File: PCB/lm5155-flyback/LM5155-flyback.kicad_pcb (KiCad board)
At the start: 2 copper layers, 2 parts, among them T1 EP7-5801_750315825, U1 LM5155

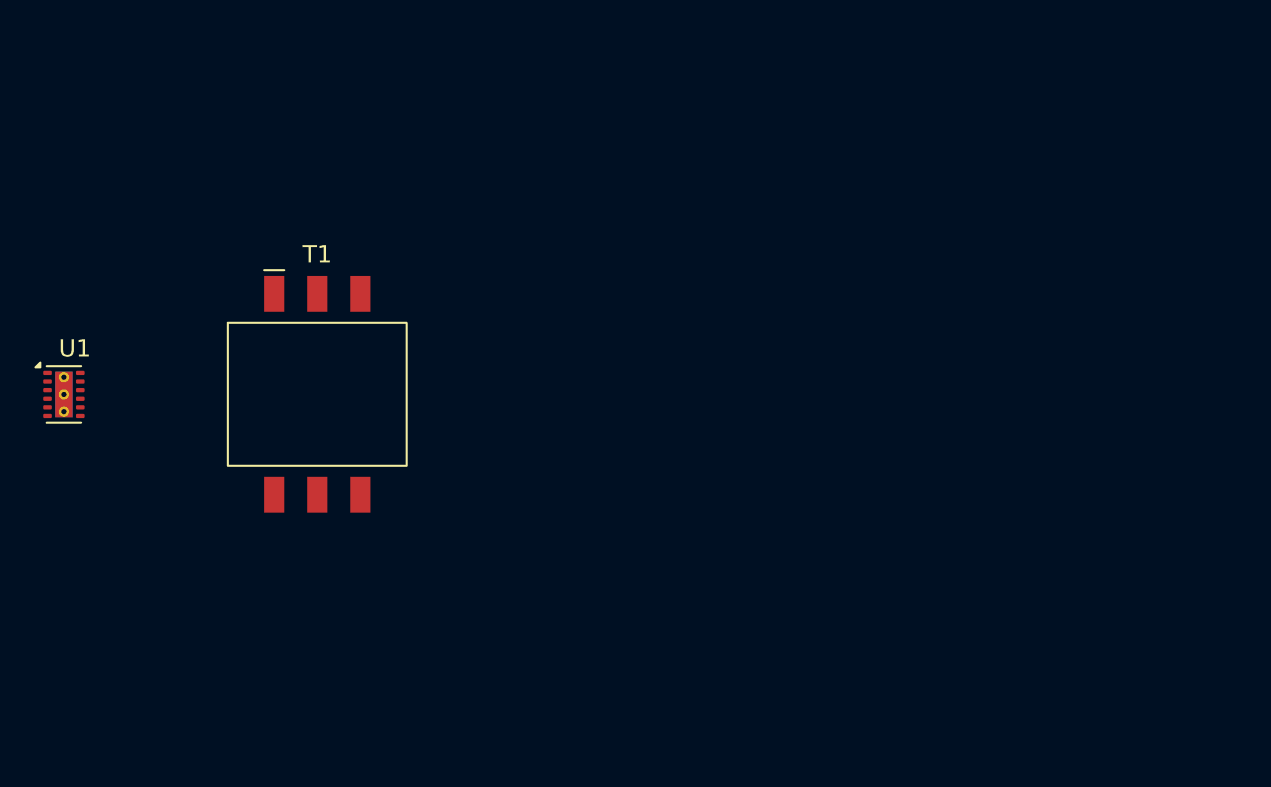
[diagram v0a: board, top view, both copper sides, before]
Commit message: Started flyback layout and tweak simulations
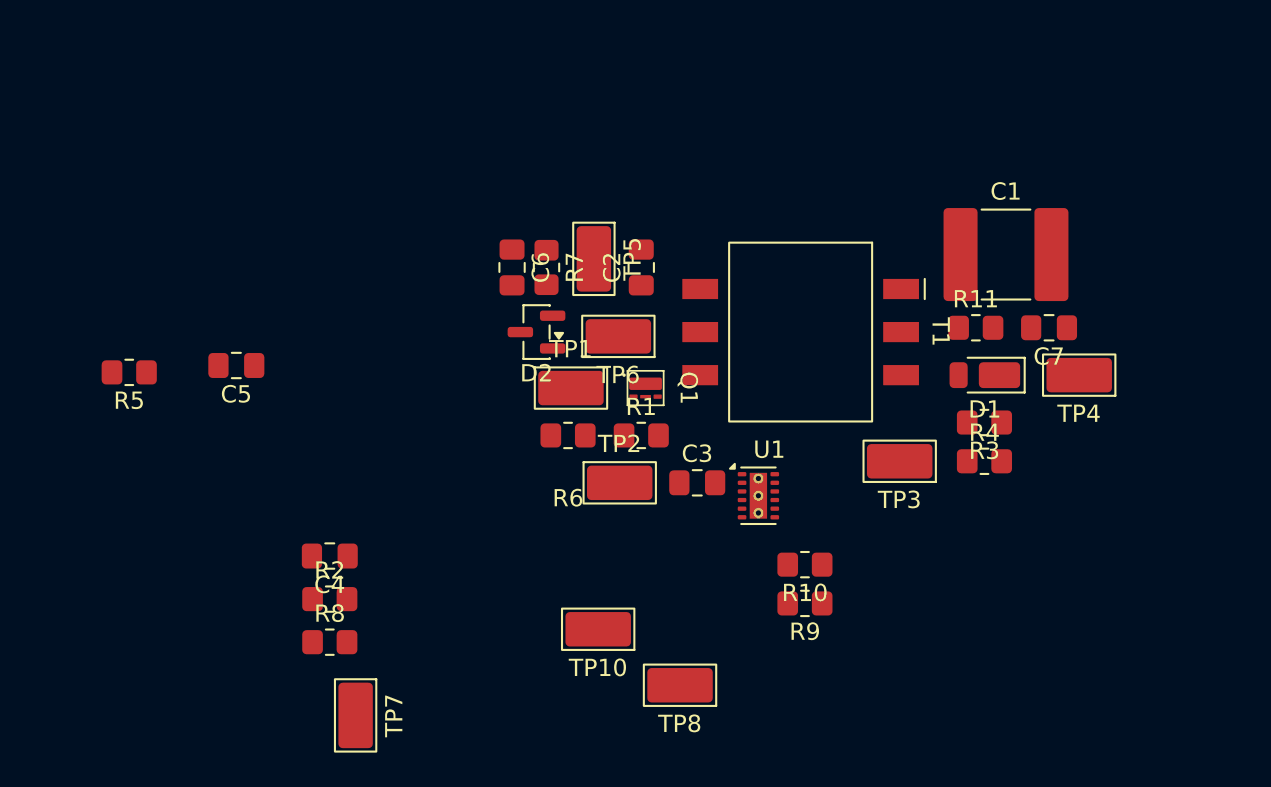
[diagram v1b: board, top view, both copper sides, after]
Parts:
- added C1: 1u, Capacitor_SMD:C_2220_5750Metric_Pad1.97x5.40mm_HandSolder, F.Cu at (192.7, 93.5)
- added C2: 4.7u, Capacitor_SMD:C_0805_2012Metric_Pad1.18x1.45mm_HandSolder, F.Cu at (171.5, 94.2)
- added C3: 1uF, Capacitor_SMD:C_0805_2012Metric_Pad1.18x1.45mm_HandSolder, F.Cu at (174.8, 106.8)
- added C4: 30n, Capacitor_SMD:C_0805_2012Metric_Pad1.18x1.45mm_HandSolder, F.Cu at (153.4, 111.0)
- added C5: 1.6n, Capacitor_SMD:C_0805_2012Metric_Pad1.18x1.45mm_HandSolder, F.Cu at (148.0, 99.9)
- added C6: 5n, Capacitor_SMD:C_0805_2012Metric_Pad1.18x1.45mm_HandSolder, F.Cu at (164.0, 94.2)
- added C7: C, Capacitor_SMD:C_0805_2012Metric_Pad1.18x1.45mm_HandSolder, F.Cu at (195.2, 97.8)
- added D1: SBR1U400P1, Diode_SMD:D_PowerDI-123, F.Cu at (191.4, 100.5)
- added D2: BAS70, Package_TO_SOT_SMD:SOT-23, F.Cu at (165.4, 98.0)
- added Q1: DMT6030LFCL-7, LM5155-flyback:U-DFN1616-6, F.Cu at (171.8, 101.2)
- added R1: 2m, Resistor_SMD:R_0805_2012Metric_Pad1.20x1.40mm_HandSolder, F.Cu at (171.5, 104.0)
- added R10: 43k, Resistor_SMD:R_0805_2012Metric_Pad1.20x1.40mm_HandSolder, F.Cu at (181.0, 111.5)
- added R11: R, Resistor_SMD:R_0805_2012Metric_Pad1.20x1.40mm_HandSolder, F.Cu at (190.9, 97.8)
- added R2: 87.5k, Resistor_SMD:R_0805_2012Metric_Pad1.20x1.40mm_HandSolder, F.Cu at (153.4, 113.5)
- added R3: 1Meg, Resistor_SMD:R_0805_2012Metric_Pad1.20x1.40mm_HandSolder, F.Cu at (191.4, 103.2)
- added R4: 5.6k, Resistor_SMD:R_0805_2012Metric_Pad1.20x1.40mm_HandSolder, F.Cu at (191.4, 105.5)
- added R5: 10k, Resistor_SMD:R_0805_2012Metric_Pad1.20x1.40mm_HandSolder, F.Cu at (141.8, 100.3)
- added R6: 1, Resistor_SMD:R_0805_2012Metric_Pad1.20x1.40mm_HandSolder, F.Cu at (167.2, 104.0)
- added R7: 3.8k, Resistor_SMD:R_0805_2012Metric_Pad1.20x1.40mm_HandSolder, F.Cu at (166.0, 94.2)
- added R8: 100k, Resistor_SMD:R_0805_2012Metric_Pad1.20x1.40mm_HandSolder, F.Cu at (153.4, 116.0)
- added R9: 82k, Resistor_SMD:R_0805_2012Metric_Pad1.20x1.40mm_HandSolder, F.Cu at (181.0, 113.8)
- added TP1: TestPoint, TestPoint:TestPoint_Keystone_5019_Miniature, F.Cu at (167.4, 101.2)
- added TP10: TestPoint, TestPoint:TestPoint_Keystone_5019_Miniature, F.Cu at (169.0, 115.2)
- added TP2: TestPoint, TestPoint:TestPoint_Keystone_5019_Miniature, F.Cu at (170.2, 106.8)
- added TP3: TestPoint, TestPoint:TestPoint_Keystone_5019_Miniature, F.Cu at (186.5, 105.5)
- added TP4: TestPoint, TestPoint:TestPoint_Keystone_5019_Miniature, F.Cu at (196.9, 100.5)
- added TP5: TestPoint, TestPoint:TestPoint_Keystone_5019_Miniature, F.Cu at (168.8, 93.8)
- added TP6: TestPoint, TestPoint:TestPoint_Keystone_5019_Miniature, F.Cu at (170.2, 98.2)
- added TP7: TestPoint, TestPoint:TestPoint_Keystone_5019_Miniature, F.Cu at (154.9, 120.2)
- added TP8: TestPoint, TestPoint:TestPoint_Keystone_5019_Miniature, F.Cu at (173.8, 118.5)
- moved U1 40.7 mm to (178.3, 107.5)
- moved T1 28.3 mm to (180.8, 98.0), turned to -90 degrees
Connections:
- net Net-(U1-BIAS) renamed /VIN
- T1 pad 4: unconnected-(T1-Pad4) -> /SW
- U1 pad 10: Net-(U1-RT) -> /RT
- U1 pad 11: unconnected-(U1-PGOOD-Pad11) -> /PGOOD
- U1 pad 12: unconnected-(U1-UVLO/EN/SYNC-Pad12) -> /UVLO
- U1 pad 3: unconnected-(U1-GATE-Pad3) -> Net-(U1-GATE)
- U1 pad 5: Net-(U1-CS) -> /CS
- U1 pad 6: unconnected-(U1-COMP-Pad6) -> /COMP
- U1 pad 9: Net-(U1-SS) -> /SS

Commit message: More flyback layout. Almost done!
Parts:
- removed TP10, TP7: TestPoint, TestPoint:TestPoint_Keystone_5019_Miniature
- moved R5 38.1 mm to (178.5, 110.5), turned to 0 degrees
- moved C5 33.0 mm to (178.5, 112.5)
- moved R2 30.6 mm to (183.8, 109.5), turned to 90 degrees
- moved R8 30.4 mm to (182.2, 106.5), turned to 180 degrees
- moved C4 28.1 mm to (181.5, 109.5), turned to -90 degrees
- moved R9 9.65 mm to (178.2, 104.5), turned to 0 degrees
- moved R10 7.11 mm to (182.2, 104.5), turned to 0 degrees
- moved TP8 6.27 mm to (174.2, 112.2)
- moved TP2 3.34 mm to (171.0, 103.5), turned to 180 degrees
- moved TP3 2.46 mm to (187.5, 107.8), turned to -90 degrees
- moved R1 2.30 mm to (171.0, 106.2), turned to 180 degrees
- moved TP1 1.61 mm to (166.0, 102.0)
- moved R6 1.50 mm to (167.2, 105.5), turned to 90 degrees
- moved C3 0.56 mm to (175.0, 107.2), turned to 90 degrees
- moved Q1 0.50 mm to (171.8, 100.8)
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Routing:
- net /FB: track 0.00 -> 15.6 mm
- net /VOUT: track 0.00 -> 15.1 mm
- net /VIN: track 0.00 -> 11.8 mm
- net Net-(U1-GATE): track 0.00 -> 11.0 mm
- net /GATE: track 0.00 -> 8.42 mm
- net /CS: track 0.00 -> 8.32 mm, vias 0 -> 2
- net Net-(D1-A): track 0.00 -> 6.09 mm
- net /COMP: track 0.00 -> 5.79 mm
- net /RT: track 0.00 -> 5.02 mm
- net Net-(D2-K): track 0.00 -> 4.93 mm
- net /SW: track 0.00 -> 4.29 mm
- net /UVLO: track 0.00 -> 3.75 mm
- net Net-(U1-VCC): track 0.00 -> 2.57 mm
- net GND: track 0.00 -> 2.57 mm
- net /SS: track 0.00 -> 2.55 mm
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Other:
- board outline added: 48 x 27.5 mm

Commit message: Layout done. Send to fabricate
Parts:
- added REF**: Symbol_HighVoltage_NoTriangle_2x5mm_Copper, Symbol:Symbol_HighVoltage_NoTriangle_2x5mm_Copper, F.Cu at (194.8, 86.8)
- added REF**: MountingHole_4mm, MountingHole:MountingHole_4mm, F.Cu at (201.2, 85.2)
- added REF**: MountingHole_4mm, MountingHole:MountingHole_4mm, F.Cu at (201.2, 111.2)
- added REF**: MountingHole_4mm, MountingHole:MountingHole_4mm, F.Cu at (162.0, 85.2)
- added REF**: OSHW-Logo_5.7x6mm_SilkScreen, Symbol:OSHW-Logo_5.7x6mm_SilkScreen, F.Cu at (169.0, 86.8)
- added REF**: MountingHole_4mm, MountingHole:MountingHole_4mm, F.Cu at (162.0, 111.2)
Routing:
- net /VIN: track 11.8 -> 34.2 mm, vias 0 -> 1
- net /VOUT: track 15.1 -> 22.8 mm, vias 0 -> 1
- net GND: track 2.57 -> 8.45 mm, vias 0 -> 30
- added copper zone on B.Cu, net GND
- added copper zone on F.Cu, net GND
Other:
- board size 48 x 27.5 mm -> 49 x 35.5 mm
- board text added: "DANGER! 180VDC!"
- board text added: "GND"
- board text added: "LM5155 NIXIE FLYBACK REV 1"
- board text added: "VIN"
- board text added: "VOUT"
